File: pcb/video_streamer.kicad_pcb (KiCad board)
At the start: 2 copper layers, 61 parts, among them U1 ICE40HX4K-144, U10 OV7670_module, U11 OV7670_module, U12 OV7670_module, U15 OV7670_module, U16 OV7670_module, U17 OV7670_module, U18 OV7670_module, U19 OV7670_module, U2 AT25SF041-SSHD, U20 OV7670_module, U3 KSZ9031RNXCA, U4 EP2C8Q208, U6 OV7670_module, U7 OV7670_module, U8 OV7670_module, U9 OV7670_module

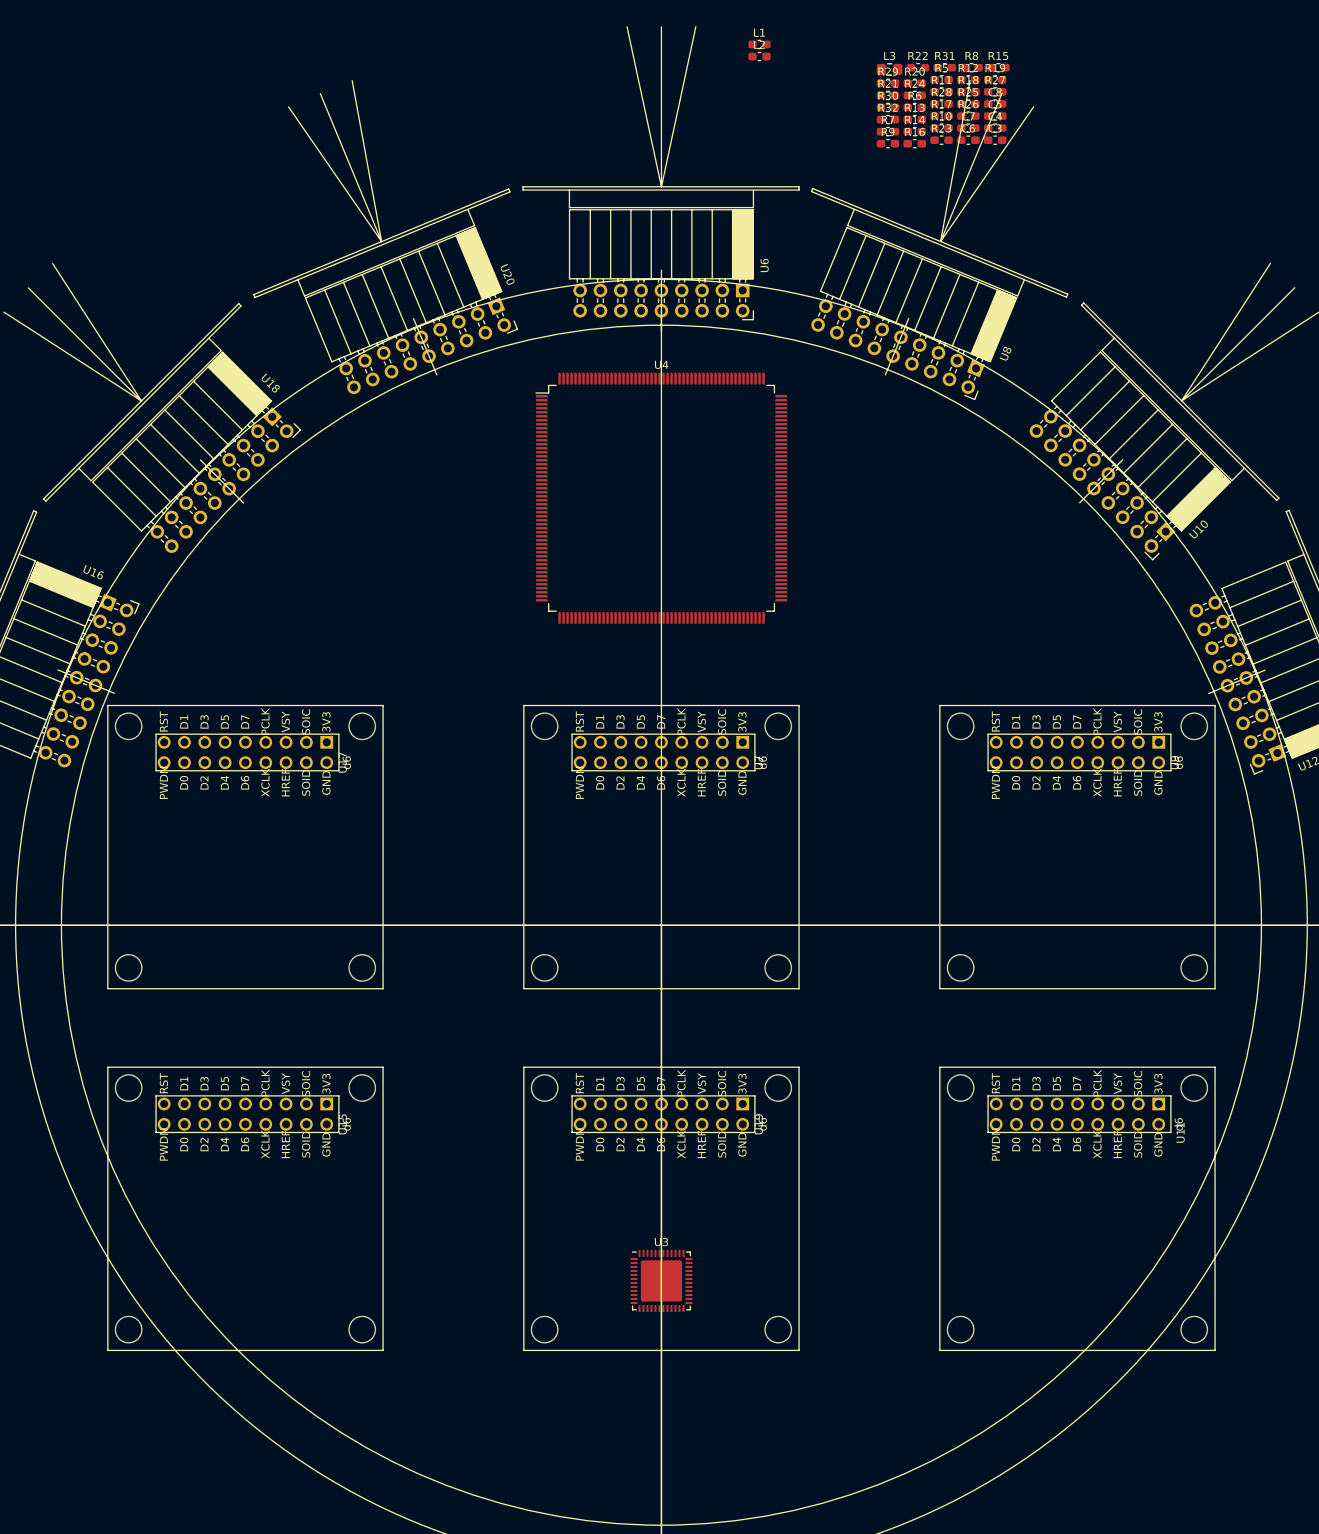
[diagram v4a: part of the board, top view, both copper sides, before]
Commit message: Update for latest EP2C8 symbol change.
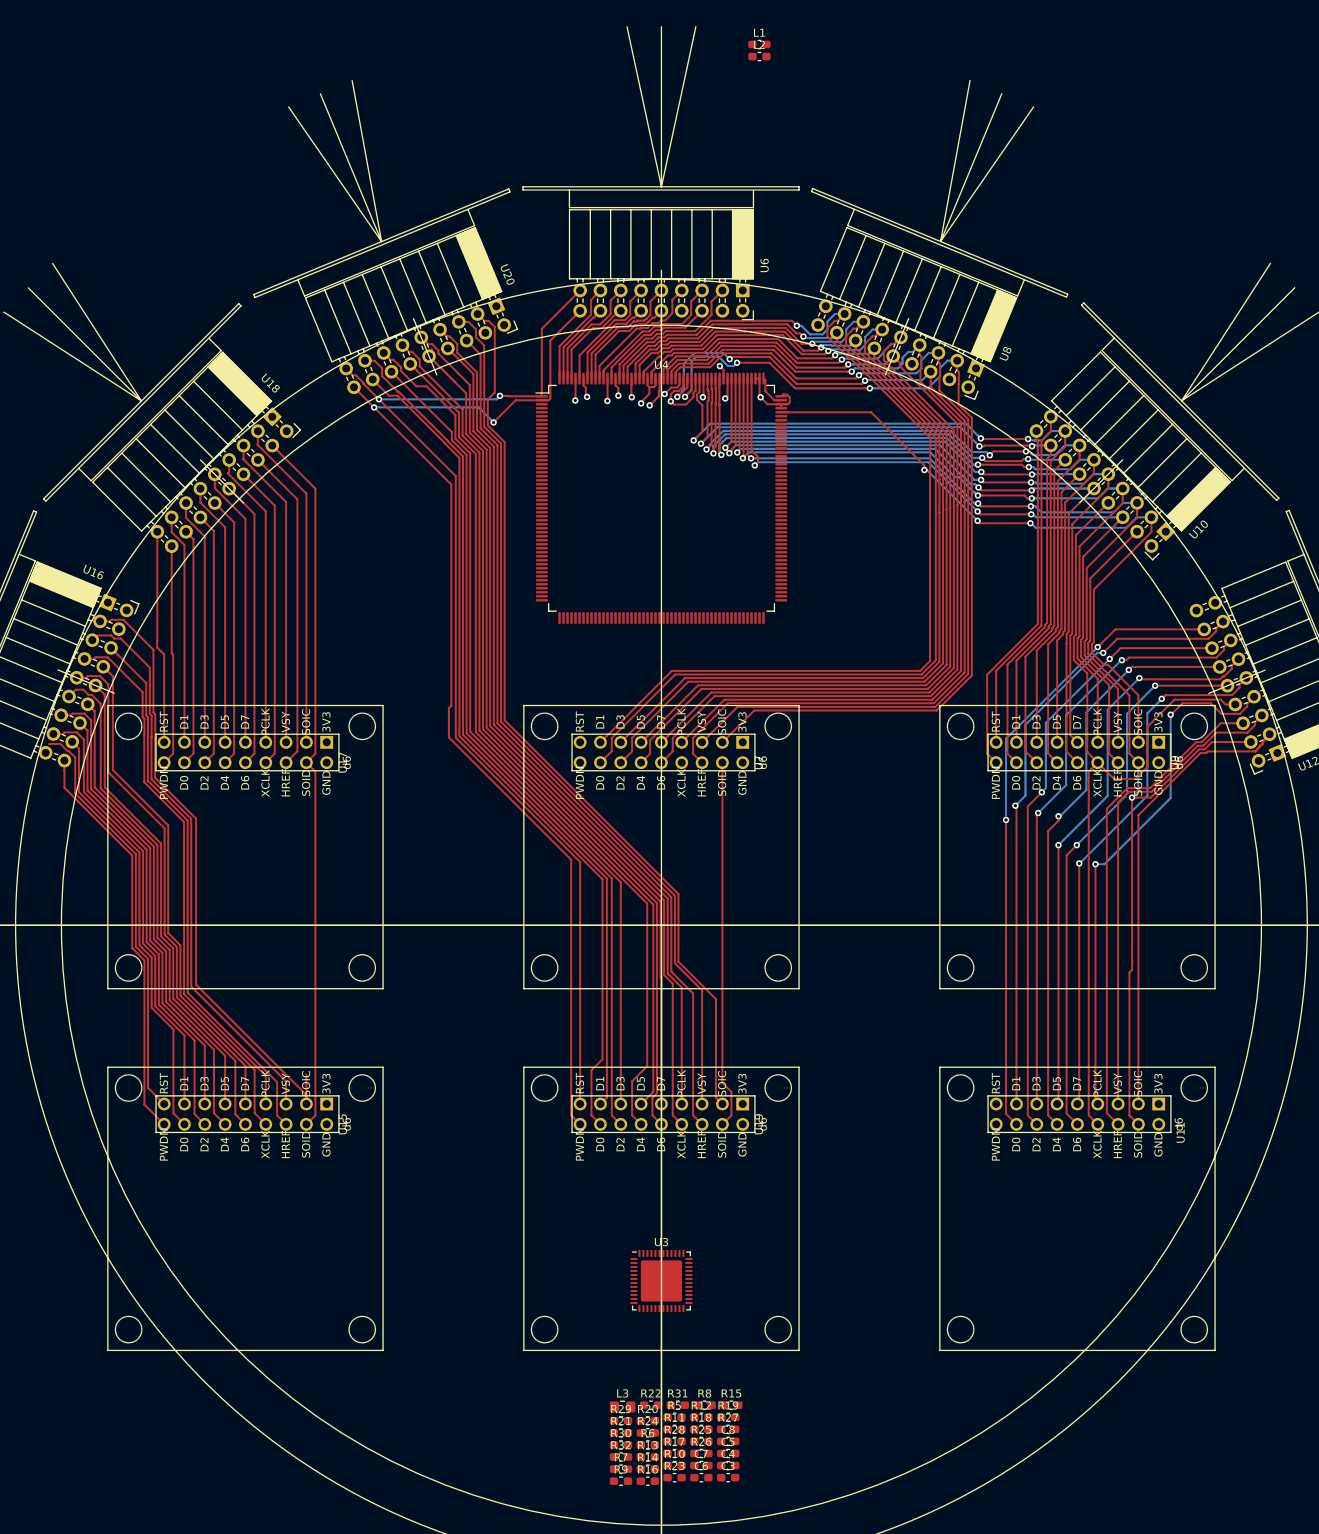
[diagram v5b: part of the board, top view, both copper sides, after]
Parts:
- moved C3 170.5 mm to (136.6, 162.8)
- moved C5 170.5 mm to (136.6, 159.8)
- moved C6 170.5 mm to (133.3, 162.8)
- moved C8 170.5 mm to (136.6, 158.3)
- moved L3 170.5 mm to (123.4, 153.9)
- moved R15 170.5 mm to (137.0, 153.7)
- moved R16 170.5 mm to (126.6, 163.2)
- moved R17 170.5 mm to (129.9, 159.8)
- moved R22 170.5 mm to (127.0, 153.7)
- moved R23 170.5 mm to (129.9, 162.8)
- moved R25 170.5 mm to (133.3, 158.3)
- moved R26 170.5 mm to (133.3, 159.8)
- moved R28 170.5 mm to (129.9, 158.3)
- moved R30 170.5 mm to (123.2, 158.7)
- moved R31 170.5 mm to (130.3, 153.7)
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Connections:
- U10 pad 10: /OV7670 Sensor 2/ov_d6 -> /EP2C8/ov2_d6
- U10 pad 11: /OV7670 Sensor 2/ov_d5 -> /EP2C8/ov2_d5
- U10 pad 12: /OV7670 Sensor 2/ov_d4 -> /EP2C8/ov2_d4
- U10 pad 13: /OV7670 Sensor 2/ov_d3 -> /EP2C8/ov2_d3
- U10 pad 14: /OV7670 Sensor 2/ov_d2 -> /EP2C8/ov2_d2
- U10 pad 15: /OV7670 Sensor 2/ov_d1 -> /EP2C8/ov2_d1
- U10 pad 16: /OV7670 Sensor 2/ov_d0 -> /EP2C8/ov2_d0
- U10 pad 9: /OV7670 Sensor 2/ov_d7 -> /EP2C8/ov2_d7
- U15 pad 10: /OV7670 Sensor 5/ov_d6 -> /OV7670 Sensor 4/ov_d6
- U15 pad 11: /OV7670 Sensor 5/ov_d5 -> /OV7670 Sensor 4/ov_d5
- U15 pad 12: /OV7670 Sensor 5/ov_d4 -> /OV7670 Sensor 4/ov_d4
- U15 pad 13: /OV7670 Sensor 5/ov_d3 -> /OV7670 Sensor 4/ov_d3
- U15 pad 14: /OV7670 Sensor 5/ov_d2 -> /OV7670 Sensor 4/ov_d2
- U15 pad 15: /OV7670 Sensor 5/ov_d1 -> /OV7670 Sensor 4/ov_d1
- U15 pad 16: /OV7670 Sensor 5/ov_d0 -> /OV7670 Sensor 4/ov_d0
- U15 pad 3: /ov5_soic -> /ov4_soic
- U15 pad 5: /ov5_vsync -> /ov4_vsync
- U15 pad 6: /ov5_href -> /ov4_href
- U15 pad 7: /ov5_pclk -> /ov4_pclk
- U15 pad 9: /OV7670 Sensor 5/ov_d7 -> /OV7670 Sensor 4/ov_d7
- U16 pad 10: /OV7670 Sensor 5/ov_d6 -> /OV7670 Sensor 4/ov_d6
- U16 pad 11: /OV7670 Sensor 5/ov_d5 -> /OV7670 Sensor 4/ov_d5
- U16 pad 12: /OV7670 Sensor 5/ov_d4 -> /OV7670 Sensor 4/ov_d4
- U16 pad 13: /OV7670 Sensor 5/ov_d3 -> /OV7670 Sensor 4/ov_d3
- U16 pad 14: /OV7670 Sensor 5/ov_d2 -> /OV7670 Sensor 4/ov_d2
- U16 pad 15: /OV7670 Sensor 5/ov_d1 -> /OV7670 Sensor 4/ov_d1
- U16 pad 16: /OV7670 Sensor 5/ov_d0 -> /OV7670 Sensor 4/ov_d0
- U16 pad 3: /ov5_soic -> /ov4_soic
- U16 pad 5: /ov5_vsync -> /ov4_vsync
- U16 pad 6: /ov5_href -> /ov4_href
- U16 pad 7: /ov5_pclk -> /ov4_pclk
- U16 pad 9: /OV7670 Sensor 5/ov_d7 -> /OV7670 Sensor 4/ov_d7
- U17 pad 10: /OV7670 Sensor 6/ov_d6 -> /OV7670 Sensor 5/ov_d6
- U17 pad 11: /OV7670 Sensor 6/ov_d5 -> /OV7670 Sensor 5/ov_d5
- U17 pad 12: /OV7670 Sensor 6/ov_d4 -> /OV7670 Sensor 5/ov_d4
- U17 pad 13: /OV7670 Sensor 6/ov_d3 -> /OV7670 Sensor 5/ov_d3
- U17 pad 14: /OV7670 Sensor 6/ov_d2 -> /OV7670 Sensor 5/ov_d2
- U17 pad 15: /OV7670 Sensor 6/ov_d1 -> /OV7670 Sensor 5/ov_d1
- U17 pad 16: /OV7670 Sensor 6/ov_d0 -> /OV7670 Sensor 5/ov_d0
- U17 pad 3: /ov6_soic -> /ov5_soic
- U17 pad 5: /ov6_vsync -> /ov5_vsync
- U17 pad 6: /ov6_href -> /ov5_href
- U17 pad 7: /ov6_pclk -> /ov5_pclk
- U17 pad 9: /OV7670 Sensor 6/ov_d7 -> /OV7670 Sensor 5/ov_d7
- U18 pad 10: /OV7670 Sensor 6/ov_d6 -> /OV7670 Sensor 5/ov_d6
- U18 pad 11: /OV7670 Sensor 6/ov_d5 -> /OV7670 Sensor 5/ov_d5
- U18 pad 12: /OV7670 Sensor 6/ov_d4 -> /OV7670 Sensor 5/ov_d4
- U18 pad 13: /OV7670 Sensor 6/ov_d3 -> /OV7670 Sensor 5/ov_d3
- U18 pad 14: /OV7670 Sensor 6/ov_d2 -> /OV7670 Sensor 5/ov_d2
- U18 pad 15: /OV7670 Sensor 6/ov_d1 -> /OV7670 Sensor 5/ov_d1
- U18 pad 16: /OV7670 Sensor 6/ov_d0 -> /OV7670 Sensor 5/ov_d0
- U18 pad 3: /ov6_soic -> /ov5_soic
- U18 pad 5: /ov6_vsync -> /ov5_vsync
- U18 pad 6: /ov6_href -> /ov5_href
- U18 pad 7: /ov6_pclk -> /ov5_pclk
- U18 pad 9: /OV7670 Sensor 6/ov_d7 -> /OV7670 Sensor 5/ov_d7
- U19 pad 10: /OV7670 Sensor 7/ov_d6 -> /OV7670 Sensor 6/ov_d6
- U19 pad 11: /OV7670 Sensor 7/ov_d5 -> /OV7670 Sensor 6/ov_d5
- U19 pad 12: /OV7670 Sensor 7/ov_d4 -> /OV7670 Sensor 6/ov_d4
- U19 pad 13: /OV7670 Sensor 7/ov_d3 -> /OV7670 Sensor 6/ov_d3
- U19 pad 14: /OV7670 Sensor 7/ov_d2 -> /OV7670 Sensor 6/ov_d2
- U19 pad 15: /OV7670 Sensor 7/ov_d1 -> /OV7670 Sensor 6/ov_d1
- U19 pad 16: /OV7670 Sensor 7/ov_d0 -> /OV7670 Sensor 6/ov_d0
- U19 pad 3: /ov7_soic -> /ov6_soic
- U19 pad 5: /ov7_vsync -> /ov6_vsync
- U19 pad 6: /ov7_href -> /ov6_href
- U19 pad 7: /ov7_pclk -> /ov6_pclk
- U19 pad 9: /OV7670 Sensor 7/ov_d7 -> /OV7670 Sensor 6/ov_d7
- U20 pad 10: /OV7670 Sensor 7/ov_d6 -> /OV7670 Sensor 6/ov_d6
- U20 pad 11: /OV7670 Sensor 7/ov_d5 -> /OV7670 Sensor 6/ov_d5
- U20 pad 12: /OV7670 Sensor 7/ov_d4 -> /OV7670 Sensor 6/ov_d4
- U20 pad 13: /OV7670 Sensor 7/ov_d3 -> /OV7670 Sensor 6/ov_d3
- U20 pad 14: /OV7670 Sensor 7/ov_d2 -> /OV7670 Sensor 6/ov_d2
- U20 pad 15: /OV7670 Sensor 7/ov_d1 -> /OV7670 Sensor 6/ov_d1
- U20 pad 16: /OV7670 Sensor 7/ov_d0 -> /OV7670 Sensor 6/ov_d0
- U20 pad 3: /ov7_soic -> /ov6_soic
- U20 pad 5: /ov7_vsync -> /ov6_vsync
- U20 pad 6: /ov7_href -> /ov6_href
- U20 pad 7: /ov7_pclk -> /ov6_pclk
- U20 pad 9: /OV7670 Sensor 7/ov_d7 -> /OV7670 Sensor 6/ov_d7
- U4 pad 1: /EP2C8/ov_reset -> /ov_reset
- U4 pad 109: Net-(U4-Pad109) -> +3V3
- U4 pad 120: Net-(U4-Pad120) -> +1V2
- U4 pad 122: Net-(U4-Pad122) -> +3V3
- U4 pad 136: Net-(U4-Pad136) -> +3V3
- U4 pad 14: Net-(U4-Pad14) -> +3V3
- U4 pad 148: Net-(U4-Pad148) -> +3V3
- U4 pad 152: Net-(U4-Pad152) -> /ov2_soic
- U4 pad 155: Net-(U4-Pad155) -> +1V2
- U4 pad 157: Net-(U4-Pad157) -> +1V2
- U4 pad 160: Net-(U4-Pad160) -> /ov2_href
- U4 pad 161: Net-(U4-Pad161) -> /ov2_vsync
- U4 pad 162: Net-(U4-Pad162) -> /ov2_pclk
- U4 pad 163: Net-(U4-Pad163) -> /EP2C8/ov2_d6
- U4 pad 164: Net-(U4-Pad164) -> /EP2C8/ov2_d7
- U4 pad 165: Net-(U4-Pad165) -> /EP2C8/ov2_d4
- U4 pad 166: Net-(U4-Pad166) -> +3V3
- U4 pad 168: Net-(U4-Pad168) -> /EP2C8/ov2_d5
- U4 pad 169: Net-(U4-Pad169) -> /EP2C8/ov2_d2
- U4 pad 170: Net-(U4-Pad170) -> /EP2C8/ov2_d3
- U4 pad 171: Net-(U4-Pad171) -> /EP2C8/ov2_d0
- U4 pad 172: Net-(U4-Pad172) -> +3V3
- U4 pad 173: Net-(U4-Pad173) -> /EP2C8/ov2_d1
- U4 pad 175: Net-(U4-Pad175) -> /ov1_soic
- U4 pad 176: Net-(U4-Pad176) -> /ov1_href
- U4 pad 178: Net-(U4-Pad178) -> +1V2
- U4 pad 179: Net-(U4-Pad179) -> /ov1_vsync
- U4 pad 180: Net-(U4-Pad180) -> /ov1_pclk
- U4 pad 181: Net-(U4-Pad181) -> /EP2C8/ov1_d6
- U4 pad 182: Net-(U4-Pad182) -> /EP2C8/ov1_d7
- U4 pad 183: Net-(U4-Pad183) -> +3V3
- U4 pad 185: Net-(U4-Pad185) -> /EP2C8/ov1_d4
- U4 pad 187: Net-(U4-Pad187) -> /EP2C8/ov1_d5
- U4 pad 188: Net-(U4-Pad188) -> /EP2C8/ov1_d2
- U4 pad 189: Net-(U4-Pad189) -> /EP2C8/ov1_d3
- U4 pad 190: Net-(U4-Pad190) -> +1V2
- U4 pad 191: Net-(U4-Pad191) -> /EP2C8/ov1_d0
- U4 pad 192: Net-(U4-Pad192) -> /EP2C8/ov1_d1
- U4 pad 193: Net-(U4-Pad193) -> /ov0_soic
- U4 pad 194: Net-(U4-Pad194) -> +3V3
- U4 pad 195: Net-(U4-Pad195) -> /ov0_href
- U4 pad 197: Net-(U4-Pad197) -> /ov0_vsync
- U4 pad 198: Net-(U4-Pad198) -> /ov0_pclk
- U4 pad 199: Net-(U4-Pad199) -> /EP2C8/ov0_d6
- U4 pad 2: Net-(U4-Pad2) -> /ov_pwdn
- U4 pad 200: Net-(U4-Pad200) -> /EP2C8/ov0_d7
- U4 pad 201: Net-(U4-Pad201) -> /EP2C8/ov0_d4
- U4 pad 202: Net-(U4-Pad202) -> +3V3
- U4 pad 203: Net-(U4-Pad203) -> /EP2C8/ov0_d5
- U4 pad 205: Net-(U4-Pad205) -> /EP2C8/ov0_d2
- U4 pad 206: Net-(U4-Pad206) -> /EP2C8/ov0_d3
- U4 pad 207: Net-(U4-Pad207) -> /EP2C8/ov0_d0
- U4 pad 208: Net-(U4-Pad208) -> /EP2C8/ov0_d1
- U4 pad 29: Net-(U4-Pad29) -> +3V3
- U4 pad 32: Net-(U4-Pad32) -> +1V2
- U4 pad 42: Net-(U4-Pad42) -> +3V3
- U4 pad 47: Net-(U4-Pad47) -> /ov_xclk
- U4 pad 51: Net-(U4-Pad51) -> +1V2
- U4 pad 53: Net-(U4-Pad53) -> +1V2
- U4 pad 62: Net-(U4-Pad62) -> +3V3
- U4 pad 66: Net-(U4-Pad66) -> +1V2
- U4 pad 7: Net-(U4-Pad7) -> +3V3
- U4 pad 71: Net-(U4-Pad71) -> +3V3
- U4 pad 79: Net-(U4-Pad79) -> +1V2
- U4 pad 83: Net-(U4-Pad83) -> +3V3
- U4 pad 91: Net-(U4-Pad91) -> +3V3
- U4 pad 98: Net-(U4-Pad98) -> +3V3
- U6 pad 10: /OV7670 Sensor 0/ov_d6 -> /EP2C8/ov0_d6
- U6 pad 11: /OV7670 Sensor 0/ov_d5 -> /EP2C8/ov0_d5
- U6 pad 12: /OV7670 Sensor 0/ov_d4 -> /EP2C8/ov0_d4
- U6 pad 13: /OV7670 Sensor 0/ov_d3 -> /EP2C8/ov0_d3
- U6 pad 14: /OV7670 Sensor 0/ov_d2 -> /EP2C8/ov0_d2
- U6 pad 15: /OV7670 Sensor 0/ov_d1 -> /EP2C8/ov0_d1
- U6 pad 16: /OV7670 Sensor 0/ov_d0 -> /EP2C8/ov0_d0
- U6 pad 9: /OV7670 Sensor 0/ov_d7 -> /EP2C8/ov0_d7
- U7 pad 10: /OV7670 Sensor 1/ov_d6 -> /EP2C8/ov1_d6
- U7 pad 11: /OV7670 Sensor 1/ov_d5 -> /EP2C8/ov1_d5
- U7 pad 12: /OV7670 Sensor 1/ov_d4 -> /EP2C8/ov1_d4
- U7 pad 13: /OV7670 Sensor 1/ov_d3 -> /EP2C8/ov1_d3
- U7 pad 14: /OV7670 Sensor 1/ov_d2 -> /EP2C8/ov1_d2
- U7 pad 15: /OV7670 Sensor 1/ov_d1 -> /EP2C8/ov1_d1
- U7 pad 16: /OV7670 Sensor 1/ov_d0 -> /EP2C8/ov1_d0
- U7 pad 9: /OV7670 Sensor 1/ov_d7 -> /EP2C8/ov1_d7
- U8 pad 10: /OV7670 Sensor 1/ov_d6 -> /EP2C8/ov1_d6
- U8 pad 11: /OV7670 Sensor 1/ov_d5 -> /EP2C8/ov1_d5
- U8 pad 12: /OV7670 Sensor 1/ov_d4 -> /EP2C8/ov1_d4
- U8 pad 13: /OV7670 Sensor 1/ov_d3 -> /EP2C8/ov1_d3
- U8 pad 14: /OV7670 Sensor 1/ov_d2 -> /EP2C8/ov1_d2
- U8 pad 15: /OV7670 Sensor 1/ov_d1 -> /EP2C8/ov1_d1
- U8 pad 16: /OV7670 Sensor 1/ov_d0 -> /EP2C8/ov1_d0
- U8 pad 9: /OV7670 Sensor 1/ov_d7 -> /EP2C8/ov1_d7
- U9 pad 10: /OV7670 Sensor 2/ov_d6 -> /EP2C8/ov2_d6
- U9 pad 11: /OV7670 Sensor 2/ov_d5 -> /EP2C8/ov2_d5
- U9 pad 12: /OV7670 Sensor 2/ov_d4 -> /EP2C8/ov2_d4
- U9 pad 13: /OV7670 Sensor 2/ov_d3 -> /EP2C8/ov2_d3
- U9 pad 14: /OV7670 Sensor 2/ov_d2 -> /EP2C8/ov2_d2
- U9 pad 15: /OV7670 Sensor 2/ov_d1 -> /EP2C8/ov2_d1
- U9 pad 16: /OV7670 Sensor 2/ov_d0 -> /EP2C8/ov2_d0
- U9 pad 9: /OV7670 Sensor 2/ov_d7 -> /EP2C8/ov2_d7
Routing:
- net /ov_xclk: track 0.00 -> 319.8 mm
- net /ov_pwdn: track 0.00 -> 263.5 mm, vias 0 -> 2
- net /ov_reset: track 0.00 -> 262.2 mm, vias 0 -> 2
- net /ov_soid: track 0.00 -> 232.5 mm, vias 0 -> 1
- net /EP2C8/ov1_d1: track 0.00 -> 129.3 mm, vias 0 -> 1
- net /EP2C8/ov1_d3: track 0.00 -> 127.3 mm, vias 0 -> 1
- net /EP2C8/ov1_d0: track 0.00 -> 125.2 mm, vias 0 -> 1
- net /EP2C8/ov1_d5: track 0.00 -> 125.0 mm, vias 0 -> 1
- net /EP2C8/ov1_d2: track 0.00 -> 123.3 mm, vias 0 -> 1
- net /ov1_href: track 0.00 -> 121.6 mm, vias 0 -> 3
- net /EP2C8/ov1_d7: track 0.00 -> 121.2 mm, vias 0 -> 1
- net /EP2C8/ov1_d4: track 0.00 -> 120.2 mm, vias 0 -> 1
- net /ov1_soic: track 0.00 -> 119.6 mm, vias 0 -> 3
- net /ov1_pclk: track 0.00 -> 117.9 mm, vias 0 -> 1
- net /EP2C8/ov1_d6: track 0.00 -> 117.5 mm, vias 0 -> 1
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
